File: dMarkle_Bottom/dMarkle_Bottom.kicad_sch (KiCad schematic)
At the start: 29 parts, among them J1 HDR_Output, J2 HDR_Input, U1 Pico, U2 74HC125, U3 74HC125, U4 74HC125, U5 74HC125

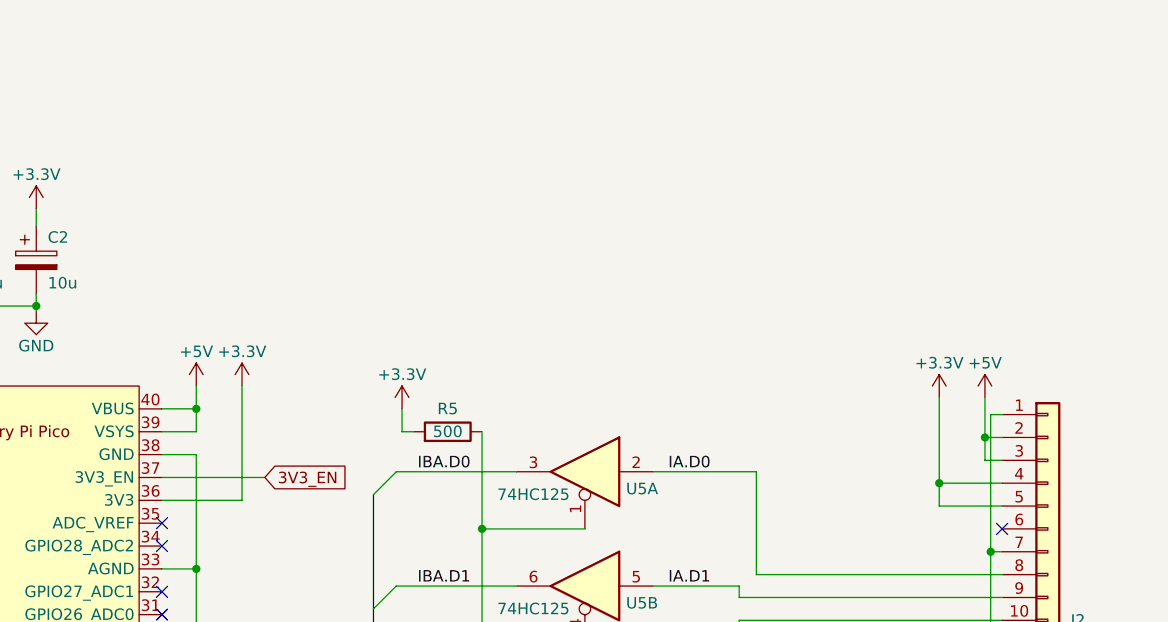
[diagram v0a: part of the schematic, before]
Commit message: Initial split of dMarkle board
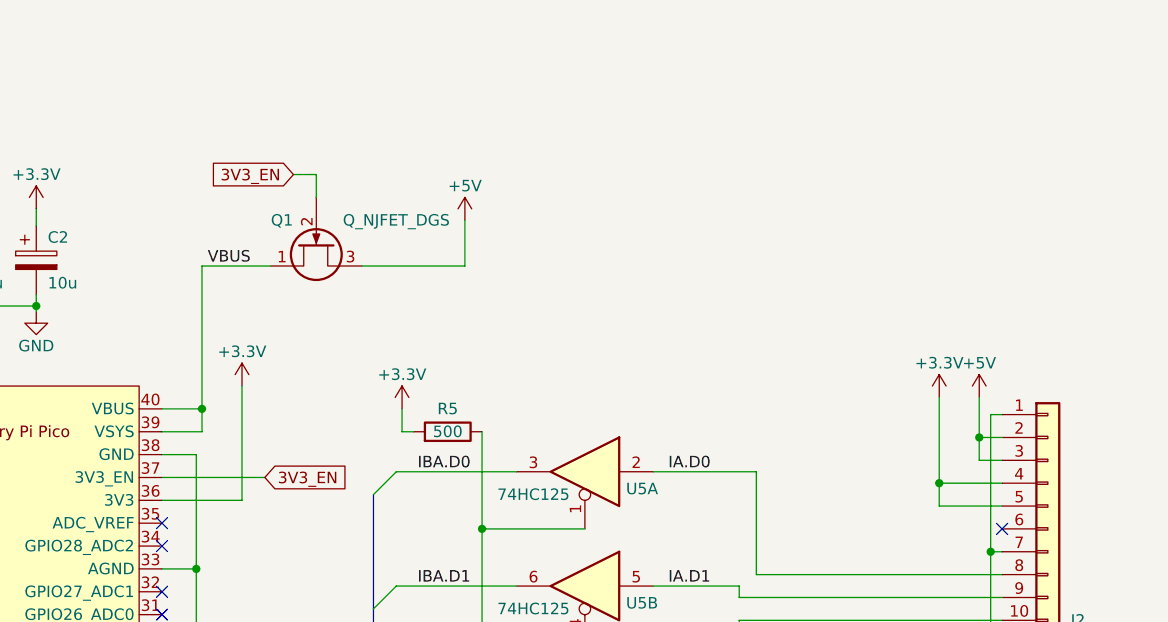
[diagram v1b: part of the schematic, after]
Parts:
- added Q1: Q_NJFET_DGS, Package_TO_SOT_THT:TO-220-3_Horizontal_TabUp, symbol Device:Q_NJFET_DGS
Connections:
- net +5V: now also Q1.3 (S); no longer U1.39 (VSYS), U1.40 (VBUS)
- net 3V3_EN: now also Q1.2 (G)
- new net VBUS: Q1.1 (D), U1.39 (VSYS), U1.40 (VBUS)
